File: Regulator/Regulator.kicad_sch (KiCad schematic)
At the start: 10 parts, among them J1 Conn_01x04, U1 LMR16006+FB

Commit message: Reverse
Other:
- title: Regualator 3.3V -> Regualator 5V
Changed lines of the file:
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@@
   (paper "A4")
   (title_block
-    (title "Regualator 3.3V")
-    (date "2021-08-07")
+    (title "Regualator 5V")
+    (date "${DATE}")
     (rev "1")
   )

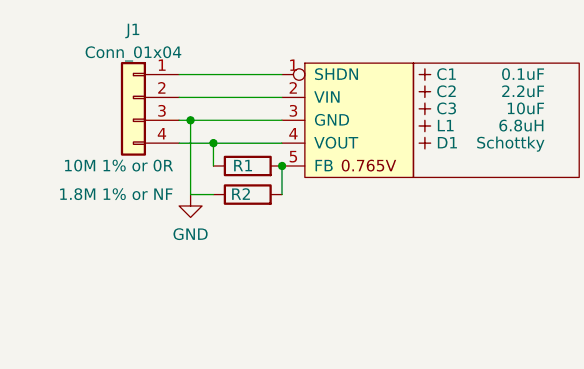
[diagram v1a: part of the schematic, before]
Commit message: Tidy up SHDN
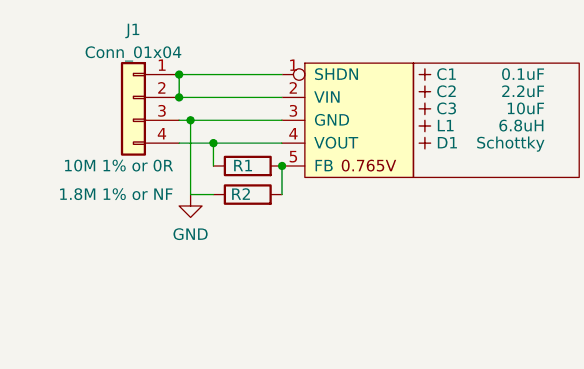
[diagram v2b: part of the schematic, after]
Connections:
- net at J1.1 (Pin_1), U1.1 (SHDN): now also J1.2 (Pin_2), U1.2 (VIN)
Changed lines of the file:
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@@
   (junction (at 100.965 65.405) (diameter 0) (color 0 0 0 0)
+  )
+  (junction (at 89.535 57.785) (diameter 0) (color 0 0 0 0)
+  )
+  (junction (at 89.535 55.245) (diameter 0) (color 0 0 0 0)
   )
   (junction (at 93.345 62.865) (diameter 0) (color 0 0 0 0)
@@
     (stroke (width 0) (type default) (color 0 0 0 0))
   )
+  (wire (pts (xy 89.535 55.245) (xy 89.535 57.785))
+    (stroke (width 0) (type default) (color 0 0 0 0))
+  )

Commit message: Tidy regulator
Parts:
- C1: value 0.1uF -> 100nF; footprint RevK:Hidden -> RevK:C_0603_
- C2, C3: footprint RevK:Hidden -> RevK:C_0805_
- D1: footprint RevK:Hidden -> RevK:D_1206_
- L1: footprint RevK:Hidden -> RevK:L_4x4_
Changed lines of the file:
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@@
       (effects (font (size 1.27 1.27)) (justify left))
     )
-    (property "Value" "0.1uF" (id 1) (at 130.175 55.245 0)
-      (effects (font (size 1.27 1.27)) (justify right))
-    )
-    (property "Footprint" "RevK:Hidden" (id 2) (at 116.84 55.245 0)
+    (property "Value" "100nF" (id 1) (at 130.175 55.245 0)
+      (effects (font (size 1.27 1.27)) (justify right))
+    )
+    (property "Footprint" "RevK:C_0603_" (id 2) (at 116.84 55.245 0)
       (effects (font (size 1.27 1.27)) hide)
     )
@@
       (effects (font (size 1.27 1.27)) (justify right))
     )
-    (property "Footprint" "RevK:Hidden" (id 2) (at 116.84 57.15 0)
+    (property "Footprint" "RevK:C_0805_" (id 2) (at 116.84 57.15 0)
       (effects (font (size 1.27 1.27)) hide)
     )
@@
       (effects (font (size 1.27 1.27)) (justify right))
     )
-    (property "Footprint" "RevK:Hidden" (id 2) (at 116.84 59.055 0)
+    (property "Footprint" "RevK:C_0805_" (id 2) (at 116.84 59.055 0)
       (effects (font (size 1.27 1.27)) hide)
     )
@@
       (effects (font (size 1.27 1.27)) (justify right))
     )
-    (property "Footprint" "RevK:Hidden" (id 2) (at 116.84 60.96 0)
+    (property "Footprint" "RevK:L_4x4_" (id 2) (at 116.84 60.96 0)
       (effects (font (size 1.27 1.27)) hide)
     )
@@
       (effects (font (size 1.27 1.27)) (justify right))
     )
-    (property "Footprint" "RevK:Hidden" (id 2) (at 116.84 62.865 0)
+    (property "Footprint" "RevK:D_1206_" (id 2) (at 116.84 62.865 0)
       (effects (font (size 1.27 1.27)) hide)
     )
@@
     )
     (path "/00000000-0000-0000-0000-0000610f9b88"
-      (reference "C1") (unit 1) (value "0.1uF") (footprint "RevK:Hidden")
+      (reference "C1") (unit 1) (value "100nF") (footprint "RevK:C_0603_")
     )
     (path "/00000000-0000-0000-0000-0000610fd0ef"
-      (reference "C2") (unit 1) (value "2.2uF") (footprint "RevK:Hidden")
+      (reference "C2") (unit 1) (value "2.2uF") (footprint "RevK:C_0805_")
     )
     (path "/00000000-0000-0000-0000-0000610fd80e"
-      (reference "C3") (unit 1) (value "10uF") (footprint "RevK:Hidden")
+      (reference "C3") (unit 1) (value "10uF") (footprint "RevK:C_0805_")
     )
     (path "/00000000-0000-0000-0000-0000610fe5d2"
-      (reference "D1") (unit 1) (value "Schottky") (footprint "RevK:Hidden")
+      (reference "D1") (unit 1) (value "Schottky") (footprint "RevK:D_1206_")
     )
     (path "/a5323771-5ccb-4d0d-b118-cd57dcc7b6cd"
@@
     )
     (path "/00000000-0000-0000-0000-0000610fe01a"
-      (reference "L1") (unit 1) (value "6.8uH") (footprint "RevK:Hidden")
+      (reference "L1") (unit 1) (value "6.8uH") (footprint "RevK:L_4x4_")
     )
     (path "/ab097fcc-5168-4497-a352-43eecc18a0c7"

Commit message: Tidy
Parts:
- U1: footprint RevK:RegulatorBlockFB -> RevK:SOT-23-Thin-6-Reg
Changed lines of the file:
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@@
       (effects (font (size 1.27 1.27)) (justify left))
     )
-    (property "Footprint" "RevK:RegulatorBlockFB" (id 2) (at 112.395 52.705 0)
+    (property "Footprint" "RevK:SOT-23-Thin-6-Reg" (id 2) (at 112.395 52.705 0)
       (effects (font (size 1.27 1.27)) hide)
     )
@@
     )
     (path "/aff7249d-1a70-46a9-947a-070a2f7d9e4a"
-      (reference "U1") (unit 1) (value "LMR16006+FB") (footprint "RevK:RegulatorBlockFB")
+      (reference "U1") (unit 1) (value "LMR16006+FB") (footprint "RevK:SOT-23-Thin-6-Reg")
     )
   )

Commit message: Part
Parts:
- U1: value LMR16006+FB -> LMR16006; Part No LMR16006YQ3 -> LMR16006X or YQ3
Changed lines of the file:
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@@
       (effects (font (size 1.27 1.27)) (justify left))
     )
-    (property "Value" "LMR16006+FB" (id 1) (at 134.62 62.0272 0)
+    (property "Value" "LMR16006" (id 1) (at 134.62 62.0272 0)
       (effects (font (size 1.27 1.27)) (justify left))
     )
@@
       (effects (font (size 1.27 1.27)) hide)
     )
-    (property "Part No" "LMR16006YQ3" (id 5) (at 100.965 55.245 0)
+    (property "Part No" "LMR16006X or YQ3" (id 5) (at 100.965 55.245 0)
       (effects (font (size 1.27 1.27)) hide)
     )
@@
     )
     (path "/aff7249d-1a70-46a9-947a-070a2f7d9e4a"
-      (reference "U1") (unit 1) (value "LMR16006+FB") (footprint "RevK:SOT-23-Thin-6-Reg")
+      (reference "U1") (unit 1) (value "LMR16006") (footprint "RevK:SOT-23-Thin-6-Reg")
     )
   )

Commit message: New production files
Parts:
- U1: value LMR16006 -> LMR16006XDDCR; LCSC Part (none) -> C87080; Manufacturer TI -> (none); Part No LMR16006X or YQ3 -> (none)
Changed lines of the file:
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@@
       (effects (font (size 1.27 1.27)) (justify left))
     )
-    (property "Value" "LMR16006" (id 1) (at 134.62 62.0272 0)
+    (property "Value" "LMR16006XDDCR" (id 1) (at 134.62 62.0272 0)
       (effects (font (size 1.27 1.27)) (justify left))
     )
@@
       (effects (font (size 1.27 1.27)) hide)
     )
-    (property "Manufacturer" "TI" (id 4) (at 100.965 55.245 0)
-      (effects (font (size 1.27 1.27)) hide)
-    )
-    (property "Part No" "LMR16006X or YQ3" (id 5) (at 100.965 55.245 0)
+    (property "LCSC Part" "C87080" (id 4) (at 100.965 55.245 0)
       (effects (font (size 1.27 1.27)) hide)
     )
@@
     )
     (path "/aff7249d-1a70-46a9-947a-070a2f7d9e4a"
-      (reference "U1") (unit 1) (value "LMR16006") (footprint "RevK:SOT-23-Thin-6-Reg")
+      (reference "U1") (unit 1) (value "LMR16006XDDCR") (footprint "RevK:SOT-23-Thin-6-Reg")
     )
   )

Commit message: Working on assembly files
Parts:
- C1: LCSC Part # (none) -> C30926
- C2: LCSC Part # (none) -> C19110
- C3: LCSC Part # (none) -> C17024
- D1: LCSC Part # (none) -> C143805; Part No CD1206-B2100 -> (none)
- J1: footprint Connector_PinHeader_2.54mm:PinHeader_1x04_P2.54mm_Vertical -> RevK:PinHeader_1x04_P2.54mm_Right; LCSC Part # (none) -> C91552
- L1: footprint RevK:L_4x4_ -> RevK:L_1210_; LCSC Part # (none) -> C560045; Manufacturer Laird -> (none); Part No TYA4020 -> (none)
- R1: value 10M 1% or 0R -> 100k 1%; LCSC Part # (none) -> C14675
- R2: value 1.8M 1% or NF -> 30k 1%; LCSC Part # (none) -> C100001
- U1: footprint RevK:SOT-23-Thin-6-Reg -> RevK:SOT-23-Thin-6-Reg2; LCSC Part C87080 -> (none); LCSC Part # (none) -> C87080
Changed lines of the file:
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@@
+      (effects (font (size 1.27 1.27)) hide)
+    )
+    (property "LCSC Part #" "C30926" (id 5) (at 116.84 55.245 0)
       (effects (font (size 1.27 1.27)) hide)
     )
@@
       (effects (font (size 1.27 1.27)) hide)
     )
+    (property "LCSC Part #" "C19110" (id 5) (at 116.84 57.15 0)
+      (effects (font (size 1.27 1.27)) hide)
+    )
     (pin "~")
   )
@@
       (effects (font (size 1.27 1.27)) hide)
     )
+    (property "LCSC Part #" "C17024" (id 5) (at 116.84 59.055 0)
+      (effects (font (size 1.27 1.27)) hide)
+    )
     (pin "~")
   )
@@
       (effects (font (size 1.27 1.27)) (justify right))
     )
-    (property "Footprint" "RevK:L_4x4_" (id 2) (at 116.84 60.96 0)
-      (effects (font (size 1.27 1.27)) hide)
-    )
-    (property "Datasheet" "https://www.mouser.co.uk/datasheet/2/987/Laird_Performance_TYA4020_series__Rev_A_-1877538.pdf" (id 3) (at 116.84 60.96 0)
-      (effects (font (size 1.27 1.27)) hide)
-    )
-    (property "Manufacturer" "Laird" (id 4) (at 116.84 60.96 0)
-      (effects (font (size 1.27 1.27)) hide)
-    )
-    (property "Part No" "TYA4020" (id 5) (at 116.84 60.96 0)
+    (property "Footprint" "RevK:L_1210_" (id 2) (at 116.84 60.96 0)
+      (effects (font (size 1.27 1.27)) hide)
+    )
+    (property "Datasheet" "" (id 3) (at 116.84 60.96 0)
+      (effects (font (size 1.27 1.27)) hide)
+    )
+    (property "LCSC Part #" "C560045" (id 6) (at 116.84 60.96 0)
       (effects (font (size 1.27 1.27)) hide)
     )
@@
       (effects (font (size 1.27 1.27)) hide)
     )
-    (property "Part No" "CD1206-B2100" (id 5) (at 116.84 62.865 0)
+    (property "LCSC Part #" "C143805" (id 6) (at 116.84 62.865 0)
       (effects (font (size 1.27 1.27)) hide)
     )
@@
       (effects (font (size 1.27 1.27)) (justify left))
     )
-    (property "Value" "10M 1% or 0R" (id 1) (at 88.9 65.405 90)
+    (property "Value" "100k 1%" (id 1) (at 88.9 65.405 90)
       (effects (font (size 1.27 1.27)) (justify left))
     )
@@
     )
     (property "Datasheet" "~" (id 3) (at 97.155 65.405 0)
+      (effects (font (size 1.27 1.27)) hide)
+    )
+    (property "LCSC Part #" "C14675" (id 4) (at 97.155 65.405 90)
       (effects (font (size 1.27 1.27)) hide)
     )
@@
     (property "Reference" "J1" (id 0) (at 84.455 50.2752 0))
     (property "Value" "Conn_01x04" (id 1) (at 84.455 52.8121 0))
-    (property "Footprint" "Connector_PinHeader_2.54mm:PinHeader_1x04_P2.54mm_Vertical" (id 2) (at 84.455 57.785 0)
+    (property "Footprint" "RevK:PinHeader_1x04_P2.54mm_Right" (id 2) (at 84.455 57.785 0)
       (effects (font (size 1.27 1.27)) hide)
     )
     (property "Datasheet" "~" (id 3) (at 84.455 57.785 0)
+      (effects (font (size 1.27 1.27)) hide)
+    )
+    (property "LCSC Part #" "C91552" (id 4) (at 84.455 57.785 0)
       (effects (font (size 1.27 1.27)) hide)
     )
@@
       (effects (font (size 1.27 1.27)) (justify left))
     )
-    (property "Footprint" "RevK:SOT-23-Thin-6-Reg" (id 2) (at 112.395 52.705 0)
-      (effects (font (size 1.27 1.27)) hide)
-    )
-    (property "Datasheet" "" (id 3) (at 112.395 52.705 0)
-      (effects (font (size 1.27 1.27)) hide)
-    )
-    (property "LCSC Part" "C87080" (id 4) (at 100.965 55.245 0)
+    (property "Footprint" "RevK:SOT-23-Thin-6-Reg2" (id 2) (at 112.395 52.705 0)
+      (effects (font (size 1.27 1.27)) hide)
+    )
+    (property "Datasheet" "~" (id 3) (at 112.395 52.705 0)
+      (effects (font (size 1.27 1.27)) hide)
+    )
+    (property "LCSC Part #" "C87080" (id 4) (at 100.965 55.245 0)
       (effects (font (size 1.27 1.27)) hide)
     )
@@
       (effects (font (size 1.27 1.27)) (justify right))
     )
-    (property "Value" "1.8M 1% or NF" (id 1) (at 88.9 68.58 90)
+    (property "Value" "30k 1%" (id 1) (at 88.9 68.58 90)
       (effects (font (size 1.27 1.27)) (justify left))
     )
@@
     )
     (property "Datasheet" "~" (id 3) (at 97.155 68.58 0)
+      (effects (font (size 1.27 1.27)) hide)
+    )
+    (property "LCSC Part #" "C100001" (id 4) (at 97.155 68.58 90)
       (effects (font (size 1.27 1.27)) hide)
     )
@@
     )
     (path "/a5323771-5ccb-4d0d-b118-cd57dcc7b6cd"
-      (reference "J1") (unit 1) (value "Conn_01x04") (footprint "Connector_PinHeader_2.54mm:PinHeader_1x04_P2.54mm_Vertical")
+      (reference "J1") (unit 1) (value "Conn_01x04") (footprint "RevK:PinHeader_1x04_P2.54mm_Right")
     )
     (path "/00000000-0000-0000-0000-0000610fe01a"
-      (reference "L1") (unit 1) (value "6.8uH") (footprint "RevK:L_4x4_")
+      (reference "L1") (unit 1) (value "6.8uH") (footprint "RevK:L_1210_")
     )
     (path "/ab097fcc-5168-4497-a352-43eecc18a0c7"
@@
     )
     (path "/256adfd0-10fb-4001-ba53-34b908fca4ce"
-      (reference "R1") (unit 1) (value "10M 1% or 0R") (footprint "RevK:R_0603")
+      (reference "R1") (unit 1) (value "100k 1%") (footprint "RevK:R_0603")
     )
     (path "/c157d72a-9058-4d2c-a239-c24f6b0b203a"
-      (reference "R2") (unit 1) (value "1.8M 1% or NF") (footprint "RevK:R_0603")
+      (reference "R2") (unit 1) (value "30k 1%") (footprint "RevK:R_0603")
     )
     (path "/aff7249d-1a70-46a9-947a-070a2f7d9e4a"
-      (reference "U1") (unit 1) (value "LMR16006XDDCR") (footprint "RevK:SOT-23-Thin-6-Reg")
-    )
-  )
+      (reference "U1") (unit 1) (value "LMR16006XDDCR") (footprint "RevK:SOT-23-Thin-6-Reg2")
+    )
+  )
